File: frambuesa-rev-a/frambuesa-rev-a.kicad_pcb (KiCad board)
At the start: 2 copper layers, 50 x 50 mm, 1 part, among them U1 RP2040

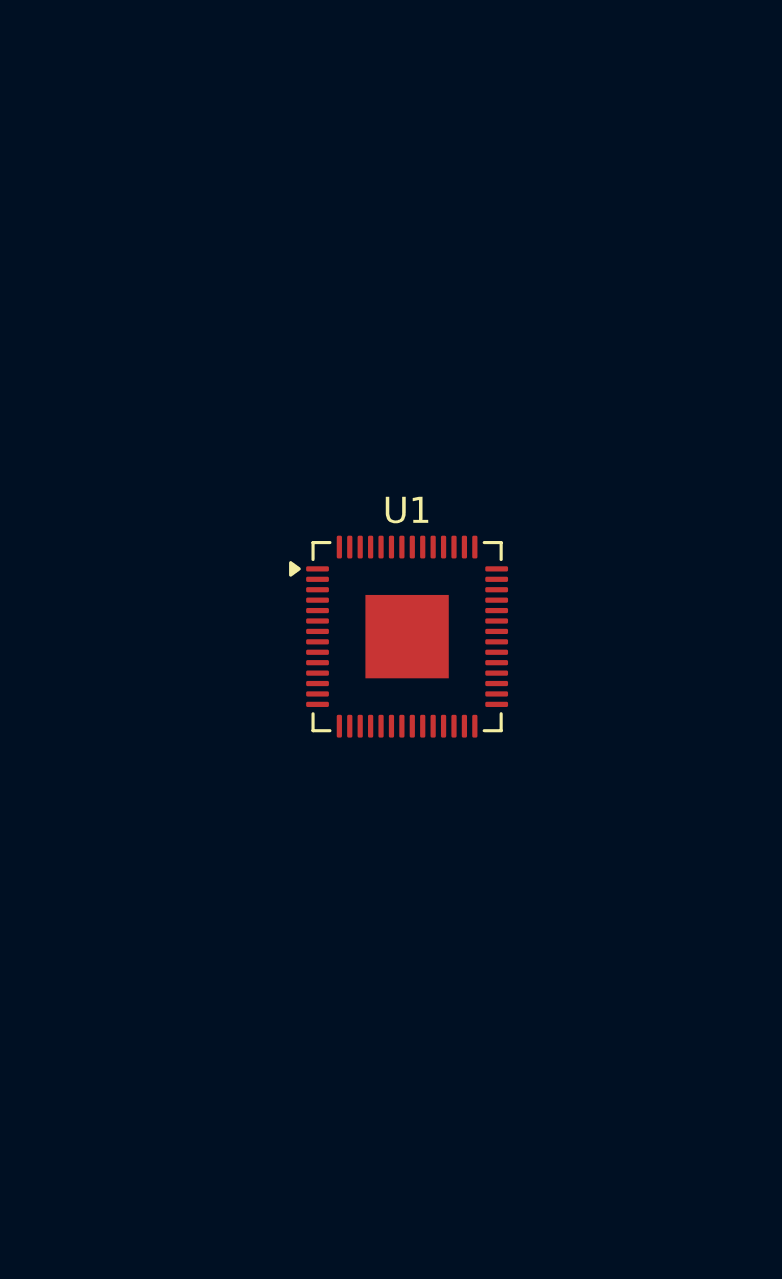
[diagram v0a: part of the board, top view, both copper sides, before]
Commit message: agregar footprints m3
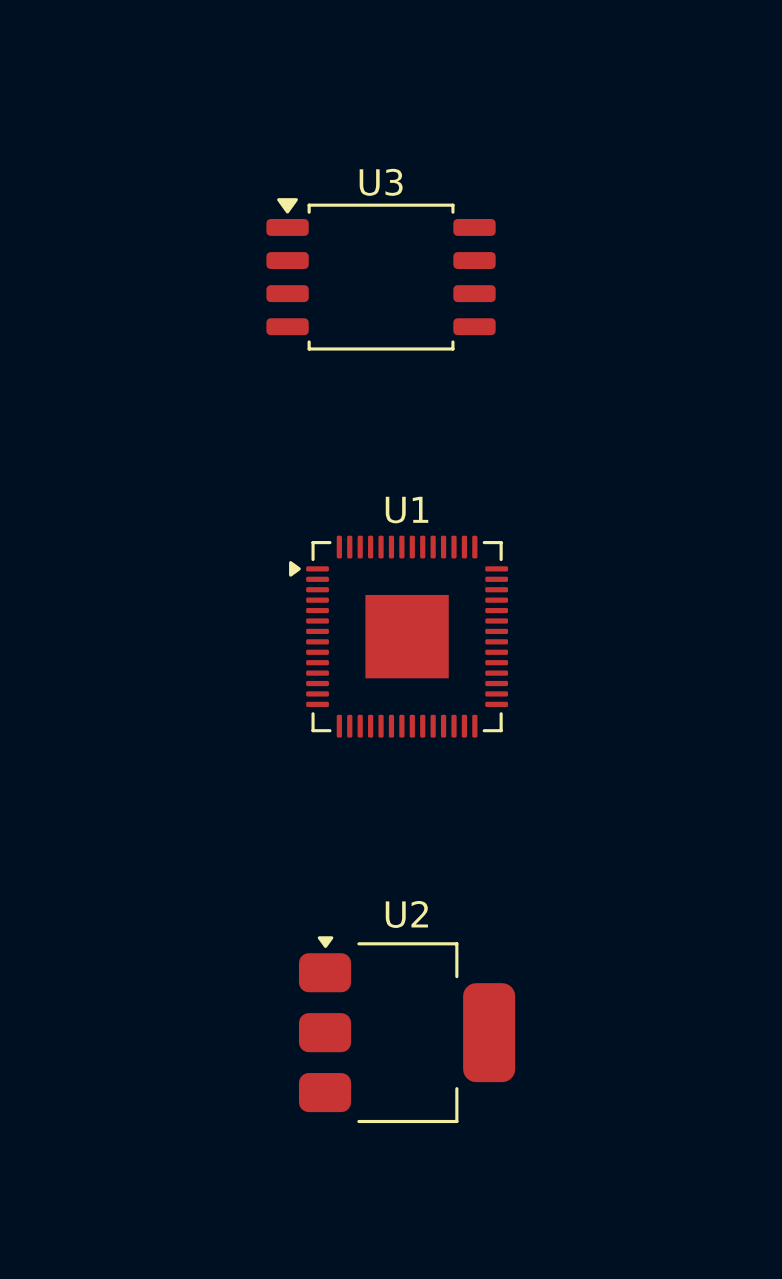
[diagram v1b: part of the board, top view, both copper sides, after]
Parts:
- added U2: NCP1117-3.3_SOT223, Package_TO_SOT_SMD:SOT-223-3_TabPin2, F.Cu at (75.0, 90.0)
- added U3: W25Q128JVS, Package_SO:SOIC-8_5.3x5.3mm_P1.27mm, F.Cu at (74.0, 61.0)
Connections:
- U1 pad 1: Net-(U1-IOVDD-Pad1) -> +3V3
- U1 pad 10: Net-(U1-IOVDD-Pad1) -> +3V3
- U1 pad 11: unconnected-(U1-GPIO8-Pad11) -> /GPIO08
- U1 pad 12: unconnected-(U1-GPIO9-Pad12) -> /GPIO09
- U1 pad 13: unconnected-(U1-GPIO10-Pad13) -> /GPIO10
- U1 pad 14: unconnected-(U1-GPIO11-Pad14) -> /GPIO11
- U1 pad 15: unconnected-(U1-GPIO12-Pad15) -> /GPIO12
- U1 pad 16: unconnected-(U1-GPIO13-Pad16) -> /GPIO13
- U1 pad 17: unconnected-(U1-GPIO14-Pad17) -> /GPIO14
- U1 pad 18: unconnected-(U1-GPIO15-Pad18) -> /GPIO15
- U1 pad 19: unconnected-(U1-TESTEN-Pad19) -> GND
- U1 pad 2: unconnected-(U1-GPIO0-Pad2) -> /GPIO00
- U1 pad 20: unconnected-(U1-XIN-Pad20) -> /XIN
- U1 pad 21: unconnected-(U1-XOUT-Pad21) -> /XOUT
- U1 pad 22: Net-(U1-IOVDD-Pad1) -> +3V3
- U1 pad 23: Net-(U1-DVDD-Pad23) -> +1V1
- U1 pad 24: unconnected-(U1-SWCLK-Pad24) -> /SWCLK
- U1 pad 25: unconnected-(U1-SWDIO-Pad25) -> /SWD
- U1 pad 26: unconnected-(U1-RUN-Pad26) -> /RUN
- U1 pad 27: unconnected-(U1-GPIO16-Pad27) -> /GPIO16
- U1 pad 28: unconnected-(U1-GPIO17-Pad28) -> /GPIO17
- U1 pad 29: unconnected-(U1-GPIO18-Pad29) -> /GPIO18
- U1 pad 3: unconnected-(U1-GPIO1-Pad3) -> /GPIO01
- U1 pad 30: unconnected-(U1-GPIO19-Pad30) -> /GPIO19
- U1 pad 31: unconnected-(U1-GPIO20-Pad31) -> /GPIO20
- U1 pad 32: unconnected-(U1-GPIO21-Pad32) -> /GPIO21
- U1 pad 33: Net-(U1-IOVDD-Pad1) -> +3V3
- U1 pad 34: unconnected-(U1-GPIO22-Pad34) -> /GPIO22
- U1 pad 35: unconnected-(U1-GPIO23-Pad35) -> /GPIO23
- U1 pad 36: unconnected-(U1-GPIO24-Pad36) -> /GPIO24
- U1 pad 37: unconnected-(U1-GPIO25-Pad37) -> /GPIO25
- U1 pad 38: unconnected-(U1-GPIO26/ADC0-Pad38) -> /GPIO26_ADC0
- U1 pad 39: unconnected-(U1-GPIO27/ADC1-Pad39) -> /GPIO27_ADC1
- U1 pad 4: unconnected-(U1-GPIO2-Pad4) -> /GPIO02
- U1 pad 40: unconnected-(U1-GPIO28/ADC2-Pad40) -> /GPIO28_ADC2
- U1 pad 41: unconnected-(U1-GPIO29/ADC3-Pad41) -> /GPIO29_ADC3
- U1 pad 42: Net-(U1-IOVDD-Pad1) -> +3V3
- U1 pad 43: unconnected-(U1-ADC_AVDD-Pad43) -> +3V3
- U1 pad 44: unconnected-(U1-VREG_VIN-Pad44) -> +3V3
- U1 pad 45: unconnected-(U1-VREG_VOUT-Pad45) -> +1V1
- U1 pad 46: unconnected-(U1-USB_DM-Pad46) -> Net-(U1-USB_DM)
- U1 pad 47: unconnected-(U1-USB_DP-Pad47) -> Net-(U1-USB_DP)
- U1 pad 48: unconnected-(U1-USB_VDD-Pad48) -> +3V3
- U1 pad 49: Net-(U1-IOVDD-Pad1) -> +3V3
- U1 pad 5: unconnected-(U1-GPIO3-Pad5) -> /GPIO03
- U1 pad 50: Net-(U1-DVDD-Pad23) -> +1V1
- U1 pad 51: unconnected-(U1-QSPI_SD3-Pad51) -> /QSPI_SD3
- U1 pad 52: unconnected-(U1-QSPI_SCLK-Pad52) -> /QSPI_SCLK
- U1 pad 53: unconnected-(U1-QSPI_SD0-Pad53) -> /QSPI_SD0
- U1 pad 54: unconnected-(U1-QSPI_SD2-Pad54) -> /QSPI_SD2
- U1 pad 55: unconnected-(U1-QSPI_SD1-Pad55) -> /QSPI_SD1
- U1 pad 56: unconnected-(U1-~{QSPI_SS}-Pad56) -> /NOT_QSPI_SS
- U1 pad 57: unconnected-(U1-GND-Pad57) -> GND
- U1 pad 6: unconnected-(U1-GPIO4-Pad6) -> /GPIO04
- U1 pad 7: unconnected-(U1-GPIO5-Pad7) -> /GPIO05
- U1 pad 8: unconnected-(U1-GPIO6-Pad8) -> /GPIO06
- U1 pad 9: unconnected-(U1-GPIO7-Pad9) -> /GPIO07

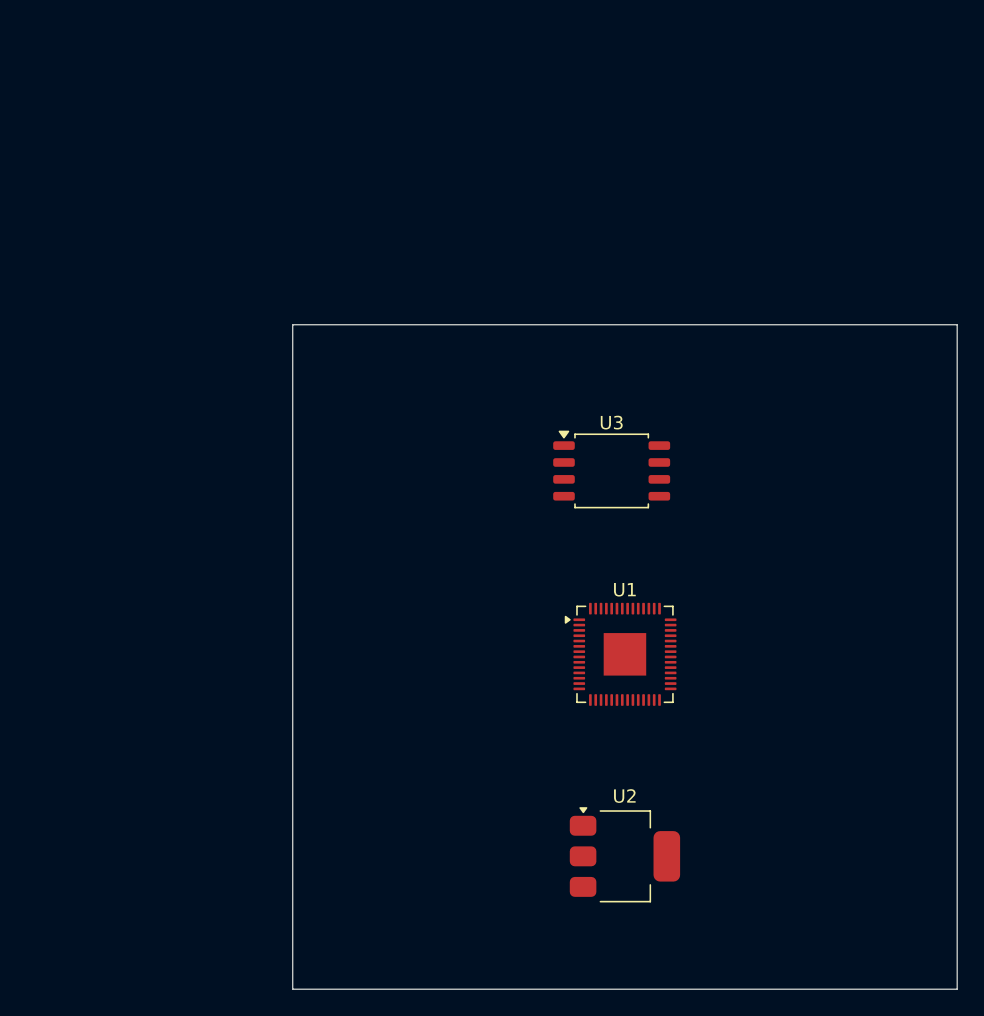
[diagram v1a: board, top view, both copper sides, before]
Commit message: cambiar tamano, borrar tracks
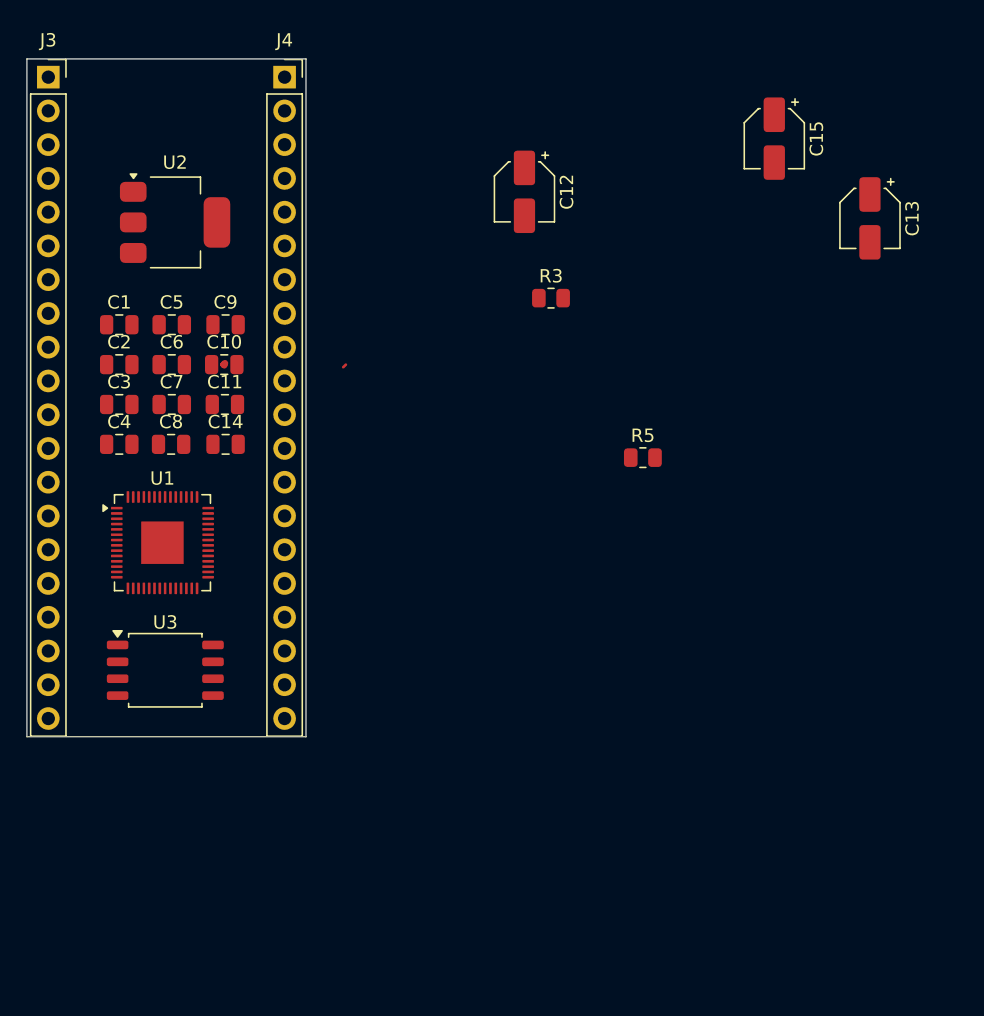
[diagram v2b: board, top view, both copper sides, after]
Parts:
- added C1: 1u, Capacitor_SMD:C_0805_2012Metric, F.Cu at (37.0, 50.0)
- added C10: 100n, Capacitor_SMD:C_0805_2012Metric, F.Cu at (44.9, 53.0)
- added C11: 100n, Capacitor_SMD:C_0805_2012Metric, F.Cu at (44.9, 56.0)
- added C12: 10u, Capacitor_SMD:CP_Elec_4x5.4, F.Cu at (67.4, 40.0)
- added C13: 10u, Capacitor_SMD:CP_Elec_4x5.4, F.Cu at (93.4, 42.0)
- added C14: 100n, Capacitor_SMD:C_0805_2012Metric, F.Cu at (45.0, 59.0)
- added C15: 10u, Capacitor_SMD:CP_Elec_4x5.4, F.Cu at (86.2, 36.0)
- added C2: 100n, Capacitor_SMD:C_0805_2012Metric, F.Cu at (37.0, 53.0)
- added C3: 100n, Capacitor_SMD:C_0805_2012Metric, F.Cu at (37.0, 56.0)
- added C4: 100n, Capacitor_SMD:C_0805_2012Metric, F.Cu at (37.0, 59.0)
- added C5: 100n, Capacitor_SMD:C_0805_2012Metric, F.Cu at (40.9, 50.0)
- added C6: 100n, Capacitor_SMD:C_0805_2012Metric, F.Cu at (40.9, 53.0)
- added C7: 100n, Capacitor_SMD:C_0805_2012Metric, F.Cu at (40.9, 56.0)
- added C8: 100n, Capacitor_SMD:C_0805_2012Metric, F.Cu at (40.9, 59.0)
- added C9: 1u, Capacitor_SMD:C_0805_2012Metric, F.Cu at (45.0, 50.0)
- added J3: Conn_02x18_Odd_Even, Connector_PinSocket_2.54mm:PinSocket_1x20_P2.54mm_Vertical, F.Cu at (31.6, 31.4)
- added J4: Conn_02x18_Odd_Even, Connector_PinSocket_2.54mm:PinSocket_1x20_P2.54mm_Vertical, F.Cu at (49.4, 31.4)
- added R3: 1k, Resistor_SMD:R_0805_2012Metric, F.Cu at (69.4, 48.0)
- added R5: 1K, Resistor_SMD:R_0805_2012Metric, F.Cu at (76.3, 60.0)
- moved U2 58.5 mm to (41.1, 42.3)
- moved U3 36.8 mm to (40.4, 76.0)
- moved U1 35.8 mm to (40.2, 66.4)
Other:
- board size 50 x 50 mm -> 21 x 51 mm
